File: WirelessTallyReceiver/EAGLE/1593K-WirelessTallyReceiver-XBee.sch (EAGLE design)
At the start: 15 parts, among them IC1 75176AP, J1 RJHSE-5381

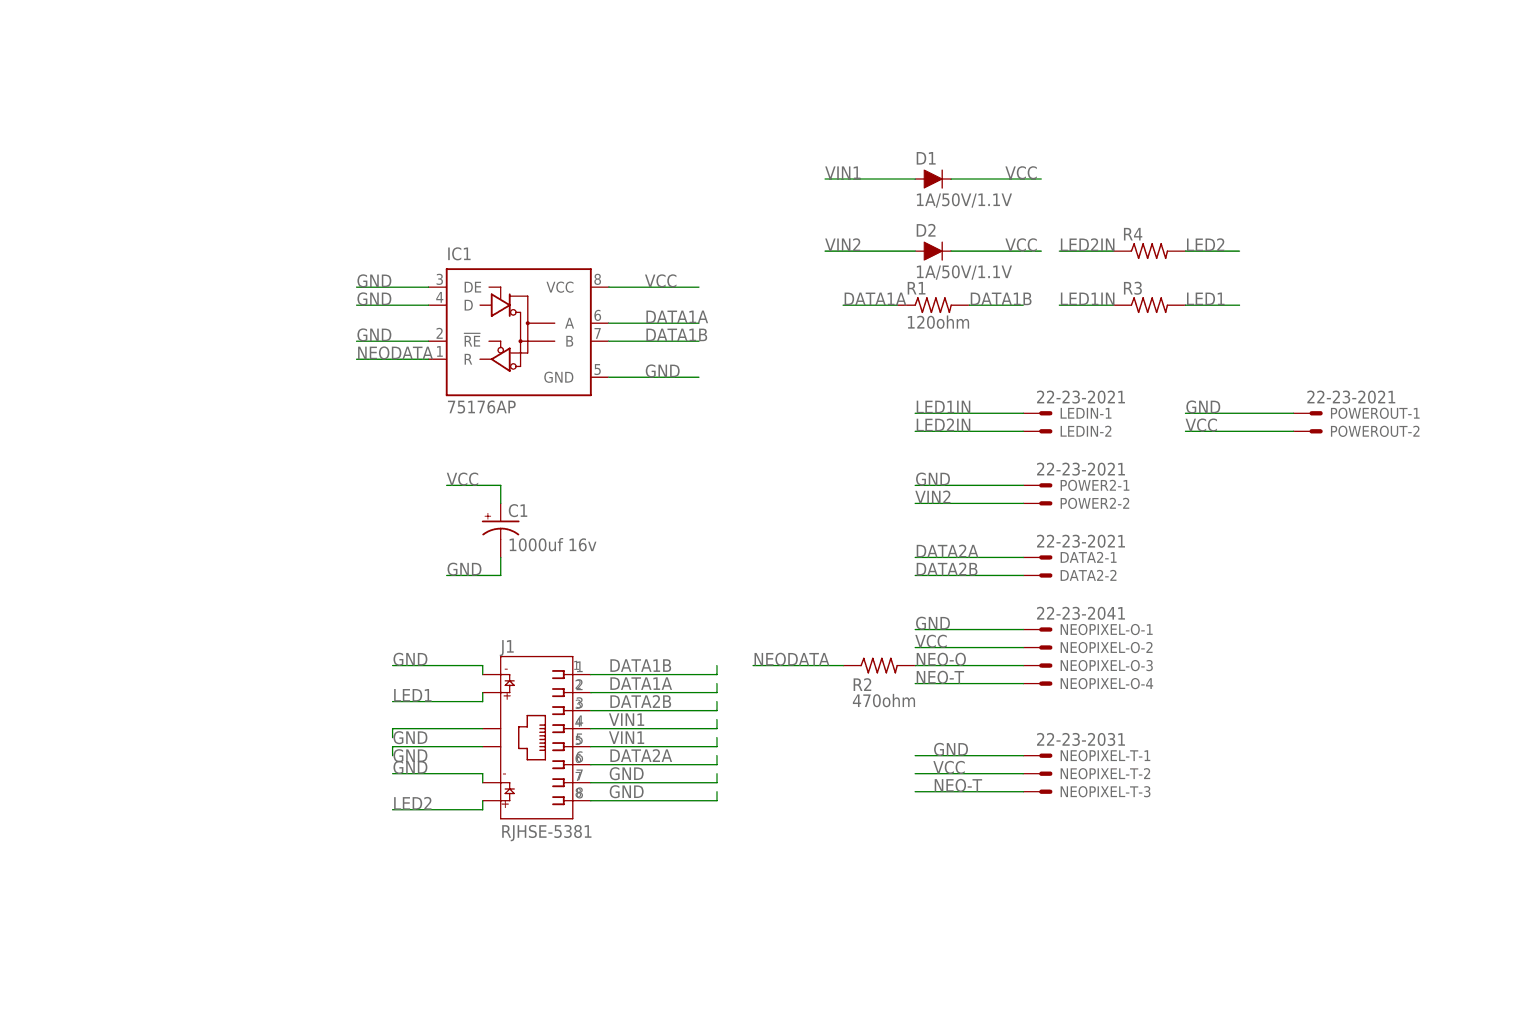
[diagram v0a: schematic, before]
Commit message: Revisions to boards after working with initial prototypes.
- Update boards to use SMD components to help save on space.
- Redesign wireless receiver to use 3.3v logic to avoid using the Xbee breakout.
- Remove designs that aren't going to be used.
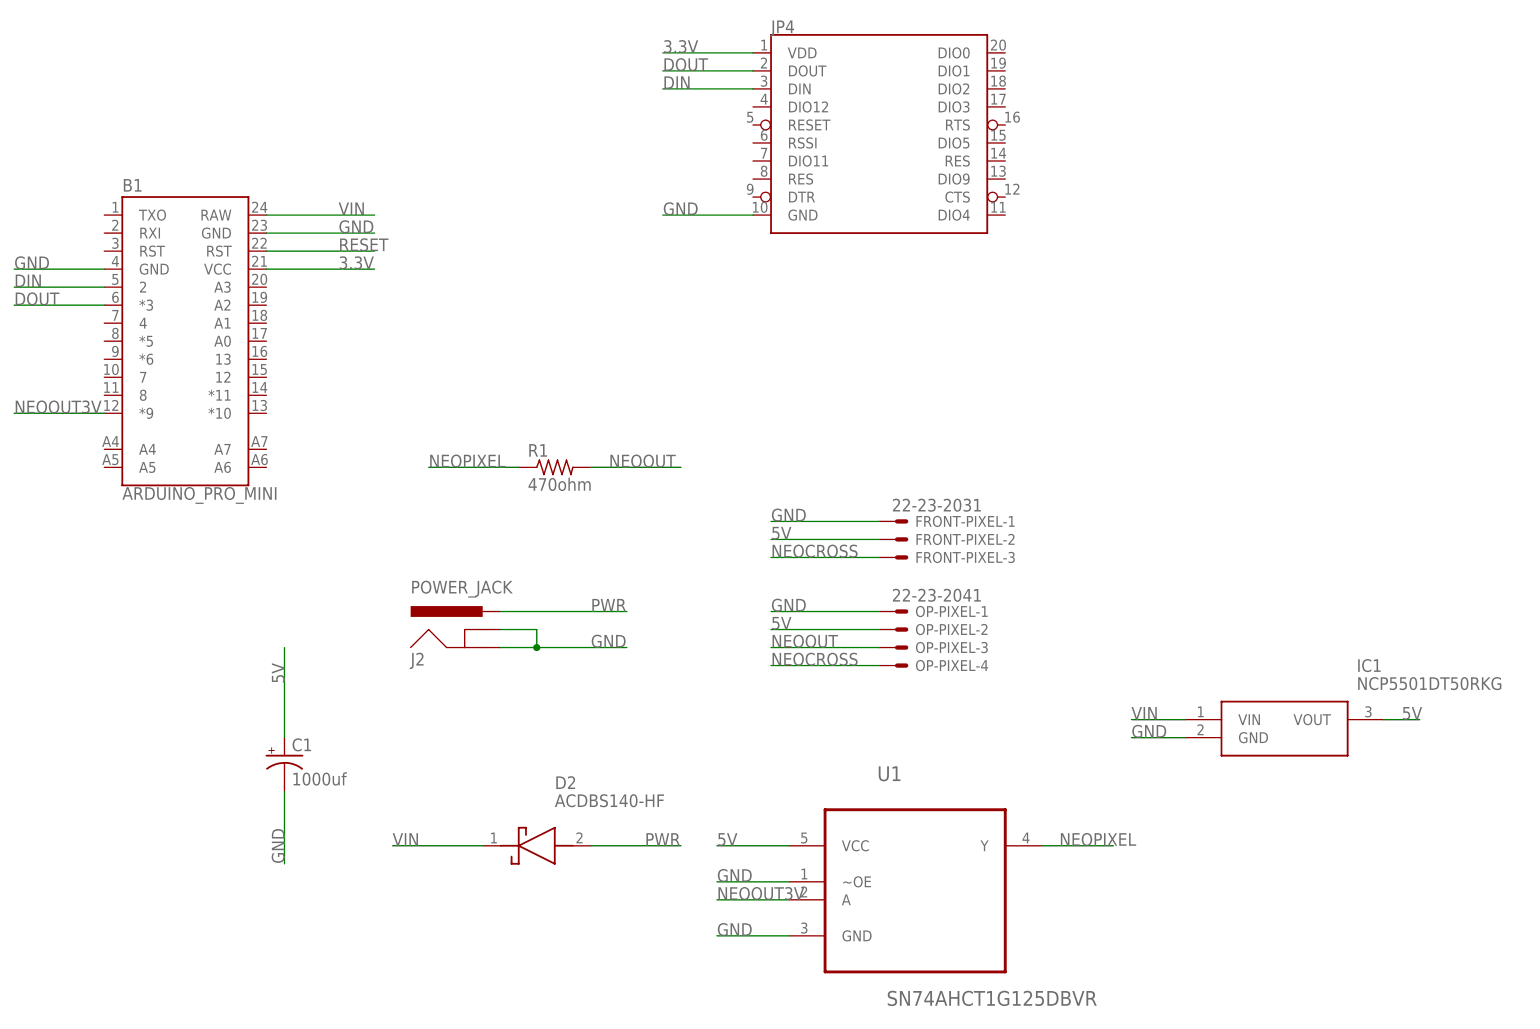
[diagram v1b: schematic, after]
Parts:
- removed D1: 1A/50V/1.1V, SparkFun-DiscreteSemi:DIODE-PTH
- removed DATA2, LEDIN, POWER2, POWEROUT: 22-23-2021, con-molex:22-23-2021
- removed J1: RJHSE-5381, RJHSE-5381:RJHSE-5381
- removed NEOPIXEL-O: 22-23-2041, con-molex:22-23-2041
- removed NEOPIXEL-T: 22-23-2031, con-molex:22-23-2031
- removed R2: 470ohm, rcl:R-US_0207/10
- removed R3, R4: (no value), rcl:R-US_0207/10
- added B1: ARDUINO_PRO_MINI, SparkFun-Boards:ARDUINO_PRO_MINI
- added FRONT-PIXEL: 22-23-2031, con-molex:22-23-2031
- added J2: POWER_JACK, SparkFun-Connectors:POWER_JACK
- added JP4: (no value), SparkFun-RF:XBEESILK
- added OP-PIXEL: 22-23-2041, con-molex:22-23-2041
- added U1: SN74AHCT1G125DBVR, Texas Instruments_By_element14_Batch_1:SN74AHCT1G125DBVR
- C1: value 1000uf 16v -> 1000uf
- D2: value 1A/50V/1.1V -> ACDBS140-HF; device SparkFun-DiscreteSemi:DIODE-PTH -> SamacSys_Parts:ACDBS140-HF
- IC1: value 75176AP -> NCP5501DT50RKG; device 751xx:75176AP -> SamacSys_Parts:NCP5501DT50RKG
- R1: value 120ohm -> 470ohm; device rcl:R-US_0207/10 -> rcl:R-US_R0805
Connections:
- removed net DATA1A: IC1.A, J1.2, R1.1
- removed net DATA1B: IC1.B, J1.1, R1.2
- removed net DATA2A: DATA2-1.S, J1.6
- removed net DATA2B: DATA2-2.S, J1.3
- removed net LED1: J1.10, R3.2
- removed net LED1IN: LEDIN-1.S, R3.1
- removed net LED2: J1.12, R4.2
- removed net LED2IN: LEDIN-2.S, R4.1
- removed net NEO-O: NEOPIXEL-O-3.S, R2.2
- removed net NEO-T: NEOPIXEL-O-4.S, NEOPIXEL-T-3.S
- removed net NEODATA: IC1.R, R2.1
- removed net VCC: C1.+, D1.C, D2.C, IC1.VCC, NEOPIXEL-O-2.S, NEOPIXEL-T-2.S, POWEROUT-2.S
- removed net VIN1: D1.A, J1.4, J1.5
- removed net VIN2: D2.A, POWER2-2.S
- new net 3.3V: B1.VCC, JP4.VDD
- new net 5V: C1.+, FRONT-PIXEL-2.S, IC1.VOUT, OP-PIXEL-2.S, U1.VCC
- new net DIN: B1.2, JP4.DIN
- new net DOUT: B1.*3, JP4.DOUT
- new net NEOCROSS: FRONT-PIXEL-3.S, OP-PIXEL-4.S
- new net NEOOUT: OP-PIXEL-3.S, R1.2
- new net NEOOUT3V: B1.*9, U1.A
- new net NEOPIXEL: R1.1, U1.Y
- new net PWR: D2.A, J2.PWR
- new net RESET: B1.RST@2
- new net VIN: B1.RAW, D2.K, IC1.VIN
- net GND: now also B1.GND, B1.GND@2, FRONT-PIXEL-1.S, J2.GND, J2.GNDBREAK, JP4.GND, OP-PIXEL-1.S, U1.GND, U1.~OE; no longer IC1.!RE, IC1.D, IC1.DE, J1.11, J1.7, J1.8, J1.9, J1.S1, J1.S2, NEOPIXEL-O-1.S, NEOPIXEL-T-1.S, POWER2-1.S, POWEROUT-1.S
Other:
- moved on the sheet: C1, R1

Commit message: Add decoupling caps
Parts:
- added C2, C3, C4, C5: (no value), Nordic_nRF:CAPACITOR_0805_N
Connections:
- net 3.3V: now also C3.1
- net 5V: now also B1.RAW, C2.1, C4.1, C5.1
- net GND: now also C2.2, C3.2, C4.2, C5.2
- net VIN: no longer B1.RAW
